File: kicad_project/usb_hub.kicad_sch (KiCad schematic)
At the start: 52 parts, among them J1 USB4105-GF-A, J2 UJ2-ADH-3-TH, U2 CY7C65632-48AXCT, U3 USBLC6-2SC6, U4 USBLC6-2SC6, U5 USBLC6-2SC6, U6 BD2221G-LBTR, U7 BD2221G-LBTR

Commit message: Friendship ended with FT232H, now CY7C652xx is my friend
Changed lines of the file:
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@@
       (effects (font (size 1.27 1.27)) hide)
     )
-    (property "Datasheet" "" (at 232.41 52.07 0)
+    (property "Datasheet" "~" (at 232.41 52.07 0)
       (effects (font (size 1.27 1.27)) hide)
     )
@@
       (effects (font (size 1.27 1.27)) hide)
     )
-    (property "Datasheet" "" (at 233.68 97.79 0)
+    (property "Datasheet" "~" (at 233.68 97.79 0)
       (effects (font (size 1.27 1.27)) hide)
     )
@@
       (effects (font (size 1.27 1.27)) (justify left) hide)
     )
-    (property "Datasheet" "https://www.cuidevices.com/product/resource/uj2-adh-th.pdf" (at 365.76 127 0)
-      (effects (font (size 1.27 1.27)) hide)
-    )
+    (property "Datasheet" " ~" (at 365.76 127 0)
+      (effects (font (size 1.27 1.27)) hide)
+    )

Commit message: Finish Rev 2 schematic, start on routing
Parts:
- added C1: 100nF, Capacitor_SMD:C_1206_3216Metric, symbol Device:C_Small
- added X1: 12.000MHz, Oscillator:Oscillator_SMD_Abracon_ASV-4Pin_7.0x5.1mm, symbol Oscillator:ASV-xxxMHz
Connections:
- net +3.3V: now also C1.2, X1.4 (Vdd)
- net 12MHZ_CLK: now also X1.3 (OUT)
- net GND: now also C1.1, X1.2 (GND)
- net ~CY7C65634_RESET renamed DATA_USB_CONNECTED
- no-connect marks 8 -> 9
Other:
- note added: "12MHz CMOS Oscillator"

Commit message: Update to KiCAD 8, start adding CAN transceiver
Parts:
- renumbered R1 to R10, R1 to R13, R1 to R14, R1 to R15, R1 to R16, R1 to R17, R1 to R18, R1 to R19, R1 to R2, R1 to R20, R1 to R21, R1 to R3, R1 to R4, R1 to R5, R1 to R6, R1 to R7, R1 to R8, R1 to R9

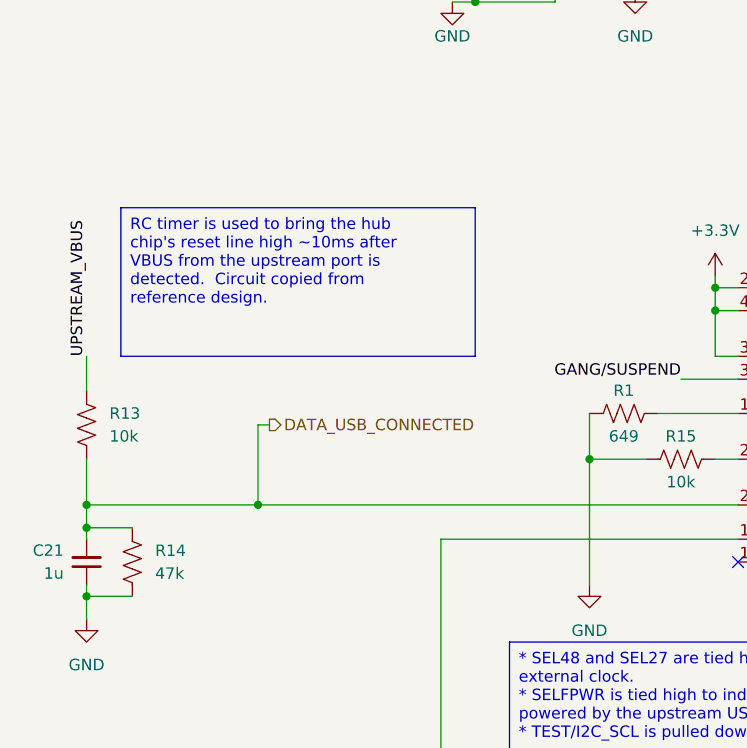
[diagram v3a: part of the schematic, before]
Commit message: Fix all known issues with v2 r2: * Invert polarity of SD card enable line to match power switch * Decrease SPI mirror resistor resistance * Pull up SD card MISO line to 3V3 * Fix reset voltage divider to output 3.3V instead of 4V * Add diode to keep reset low while power is unplugged * Move analog in to A3 instead of A0
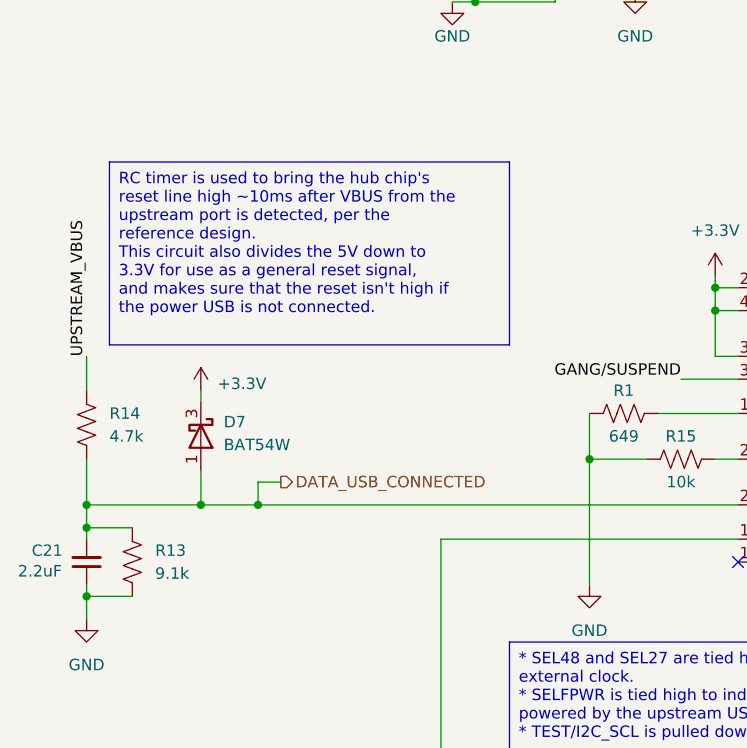
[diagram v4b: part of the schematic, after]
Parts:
- added D7: BAT54W, Package_TO_SOT_SMD:SOT-323_SC-70, symbol Diode:BAT54W
- C21: value 1u -> 2.2uF; LibRef CL31B105KBHNNNE -> CL31B225KBHNNNE; SKU (none) -> 1276-1291-1-ND
- R13: value 10k -> 9.1k; LibRef ERJ-8ENF1002V -> ERJ-8ENF9101V; SKU P10.0KFCT-ND -> P9.10KFCT-ND
- R14: value 47k -> 4.7k; SKU P47.0KFCT-ND -> P4.70KFCT-ND
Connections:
- net +3.3V: now also D7.3 (K)
- net DATA_USB_CONNECTED: now also R13.1, R14.2, D7.1 (A); no longer R13.2, R14.1
- net GND: now also R13.2; no longer R14.2
- net UPSTREAM_VBUS: now also R14.1; no longer R13.1

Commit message: Start adding CAN support... ~75% done with schematics
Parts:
- D7: SKU (none) -> 4878-BAT54WCT-ND; Supplier (none) -> Digi-Key
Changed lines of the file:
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@@
 			)
 		)
-		(property "Description" ""
+		(property "Description" "Power symbol creates a global label with name \"GND\" , ground"
 			(at 232.41 58.42 0)
 			(effects
@@
 			)
 		)
-		(property "Description" ""
+		(property "Description" "Power symbol creates a global label with name \"GND\" , ground"
 			(at 151.13 59.69 0)
 			(effects
@@
 			)
 		)
-		(property "Description" ""
+		(property "Description" "Power symbol creates a global label with name \"GND\" , ground"
 			(at 375.92 83.82 0)
 			(effects
@@
 			)
 		)
-		(property "Description" ""
+		(property "Description" "Power symbol creates a global label with name \"GND\" , ground"
 			(at 218.44 58.42 0)
 			(effects
@@
 			)
 		)
-		(property "Description" ""
+		(property "Description" "Power symbol creates a global label with name \"GND\" , ground"
 			(at 325.12 168.91 0)
 			(effects
@@
 			)
 		)
-		(property "Description" ""
+		(property "Description" "Special symbol for telling ERC where power comes from"
 			(at 58.42 68.58 0)
 			(effects
@@
 			)
 		)
-		(property "Description" ""
+		(property "Description" "Power symbol creates a global label with name \"+5V\""
 			(at 156.21 90.17 0)
 			(effects
@@
 			)
 		)
-		(property "Description" ""
+		(property "Description" "Special symbol for telling ERC where power comes from"
 			(at 238.76 46.99 0)
 			(effects
@@
 			)
 		)
-		(property "Description" ""
+		(property "Description" "Power symbol creates a global label with name \"GND\" , ground"
 			(at 373.38 147.32 0)
 			(effects
@@
 			)
 		)
-		(property "Description" ""
+		(property "Description" "Power symbol creates a global label with name \"+5V\""
 			(at 151.13 44.45 0)
 			(effects
@@
 			)
 		)
-		(property "Description" ""
+		(property "Description" "Power symbol creates a global label with name \"GND\" , ground"
 			(at 24.13 143.51 0)
 			(effects
@@
 			)
 		)
-		(property "Description" ""
+		(property "Description" "Power symbol creates a global label with name \"+3.3V\""
 			(at 217.17 201.93 0)
 			(effects
@@
 			)
 		)
-		(property "Description" ""
+		(property "Description" "Power symbol creates a global label with name \"+3.3V\""
 			(at 36.83 118.11 0)
 			(effects
@@
 			)
 		)
-		(property "Description" ""
+		(property "Description" "Power symbol creates a global label with name \"GND\" , ground"
 			(at 327.66 232.41 0)
 			(effects
@@
 			)
 		)
-		(property "Description" ""
+		(property "Description" "Power symbol creates a global label with name \"GND\" , ground"
 			(at 344.17 49.53 0)
 			(effects
@@
 			)
 		)
+		(property "SKU" "4878-BAT54WCT-ND"
+			(at 36.83 123.19 0)
+			(effects
+				(font
+					(size 1.27 1.27)
+				)
+				(hide yes)
+			)
+		)
+		(property "Supplier" "Digi-Key"
+			(at 36.83 123.19 0)
+			(effects
+				(font
+					(size 1.27 1.27)
+				)
+				(hide yes)
+			)
+		)
 		(pin "1"
 		)
@@
 			)
 		)
-		(property "Description" ""
+		(property "Description" "Power symbol creates a global label with name \"GND\" , ground"
 			(at 156.21 105.41 0)
 			(effects
@@
 			)
 		)
-		(property "Description" ""
+		(property "Description" "Power symbol creates a global label with name \"GND\" , ground"
 			(at 85.09 73.66 0)
 			(effects
@@
 			)
 		)
-		(property "Description" ""
+		(property "Description" "Power symbol creates a global label with name \"+3.3V\""
 			(at 198.12 113.03 0)
 			(effects
@@
 			)
 		)
-		(property "Description" ""
+		(property "Description" "Power symbol creates a global label with name \"GND\" , ground"
 			(at 212.09 220.98 0)
 			(effects
@@
 			)
 		)
-		(property "Description" ""
+		(property "Description" "Power symbol creates a global label with name \"GND\" , ground"
 			(at 64.77 74.93 0)
 			(effects
@@
 			)
 		)
-		(property "Description" ""
+		(property "Description" "Power symbol creates a global label with name \"+3.3V\""
 			(at 241.3 213.36 0)
 			(effects
@@
 			)
 		)
-		(property "Description" ""
+		(property "Description" "Power symbol creates a global label with name \"+3.3V\""
 			(at 218.44 236.22 0)
 			(effects
@@
 			)
 		)
-		(property "Description" ""
+		(property "Description" "Power symbol creates a global label with name \"GND\" , ground"
 			(at 213.36 254 0)
 			(effects
@@
 			)
 		)
-		(property "Description" ""
+		(property "Description" "Power symbol creates a global label with name \"+3.3V\""
 			(at 44.45 67.31 0)
 			(effects
@@
 			)
 		)
-		(property "Description" ""
+		(property "Description" "Special symbol for telling ERC where power comes from"
 			(at 240.03 92.71 0)
 			(effects
@@
 			)
 		)
-		(property "Description" ""
+		(property "Description" "Power symbol creates a global label with name \"GND\" , ground"
 			(at 68.58 243.84 0)
 			(effects
@@
 			)
 		)
-		(property "Description" ""
+		(property "Description" "Power symbol creates a global label with name \"GND\" , ground"
 			(at 58.42 63.5 0)
 			(effects
@@
 			)
 		)
-		(property "Description" ""
+		(property "Description" "Power symbol creates a global label with name \"+3.3V\""
 			(at 198.12 66.04 0)
 			(effects
@@
 			)
 		)
-		(property "Description" ""
+		(property "Description" "Power symbol creates a global label with name \"GND\" , ground"
 			(at 325.12 129.54 0)
 			(effects
@@
 			)
 		)
-		(property "Description" ""
+		(property "Description" "Power symbol creates a global label with name \"GND\" , ground"
 			(at 323.85 72.39 0)
 			(effects
@@
 			)
 		)
-		(property "Description" ""
+		(property "Description" "Power symbol creates a global label with name \"GND\" , ground"
 			(at 218.44 102.87 0)
 			(effects
@@
 			)
 		)
-		(property "Description" ""
+		(property "Description" "Power symbol creates a global label with name \"GND\" , ground"
 			(at 233.68 102.87 0)
 			(effects
@@
 			)
 		)
-		(property "Description" ""
+		(property "Description" "Power symbol creates a global label with name \"GND\" , ground"
 			(at 39.37 186.69 0)
 			(effects
@@
 			)
 		)
-		(property "Description" ""
+		(property "Description" "Power symbol creates a global label with name \"+3.3V\""
 			(at 93.98 105.41 0)
 			(effects
@@
 			)
 		)
-		(property "Description" ""
+		(property "Description" "Special symbol for telling ERC where power comes from"
 			(at 71.12 48.26 0)
 			(effects
@@
 			)
 		)
-		(property "Description" ""
+		(property "Description" "Power symbol creates a global label with name \"+3.3V\""
 			(at 24.13 165.1 0)
 			(effects
@@
 			)
 		)
-		(property "Description" ""
+		(property "Description" "Power symbol creates a global label with name \"GND\" , ground"
 			(at 80.01 139.7 0)
 			(effects
@@
 			)
 		)
-		(property "Datasheet" " ~"
+		(property "Datasheet" "~"
 			(at 365.76 127 0)
 			(effects
@@
 			)
 		)
-		(property "Description" ""
+		(property "Description" "Power symbol creates a global label with name \"+3.3V\""
 			(at 58.42 36.83 0)
 			(effects

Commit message: ERC passing!
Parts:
- J1: symbol Connector:USB_C_Receptacle_USB2.0 -> Connector:USB_C_Receptacle_USB2.0_16P
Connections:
- net D1+: now also U4.6 (I/O1); no longer U4.4 (I/O2)
- net D1-: now also U4.1 (I/O1); no longer U4.6 (I/O1)
- net D2+: now also U5.6 (I/O1); no longer U5.4 (I/O2)
- net D2-: now also U5.1 (I/O1); no longer U5.6 (I/O1)
- net PREFILT_D1+: now also U4.4 (I/O2); no longer U4.3 (I/O2)
- net PREFILT_D1-: now also U4.3 (I/O2); no longer U4.1 (I/O1)
- net PREFILT_D2+: now also U5.4 (I/O2); no longer U5.3 (I/O2)
- net PREFILT_D2-: now also U5.3 (I/O2); no longer U5.1 (I/O1)
- net UPSTREAM_D+: now also U3.6 (I/O1); no longer U3.4 (I/O2)
- net UPSTREAM_D-: now also U3.1 (I/O1); no longer U3.6 (I/O1)
- net US_PREFILT_D+: now also U3.4 (I/O2); no longer U3.3 (I/O2)
- net US_PREFILT_D-: now also U3.3 (I/O2); no longer U3.1 (I/O1)

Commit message: Finish routing
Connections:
- net D1+: now also U4.4 (I/O2); no longer U4.6 (I/O1)
- net D1-: now also U4.6 (I/O1); no longer U4.1 (I/O1)
- net D2+: now also U5.4 (I/O2); no longer U5.6 (I/O1)
- net D2-: now also U5.6 (I/O1); no longer U5.1 (I/O1)
- net PREFILT_D1+: now also U4.3 (I/O2); no longer U4.4 (I/O2)
- net PREFILT_D1-: now also U4.1 (I/O1); no longer U4.3 (I/O2)
- net PREFILT_D2+: now also U5.3 (I/O2); no longer U5.4 (I/O2)
- net PREFILT_D2-: now also U5.1 (I/O1); no longer U5.3 (I/O2)
- net UPSTREAM_D+: now also U3.4 (I/O2); no longer U3.6 (I/O1)
- net UPSTREAM_D-: now also U3.6 (I/O1); no longer U3.1 (I/O1)
- net US_PREFILT_D+: now also U3.3 (I/O2); no longer U3.4 (I/O2)
- net US_PREFILT_D-: now also U3.1 (I/O1); no longer U3.3 (I/O2)

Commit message: Cleanups and more documentation
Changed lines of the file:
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@@
 	(title_block
 		(title "USB Hub")
+		(comment 1 "USB hub with 2 internal and 2 external ports.")
 	)
 	(junction
